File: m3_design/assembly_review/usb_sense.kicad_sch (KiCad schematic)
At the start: 3 parts

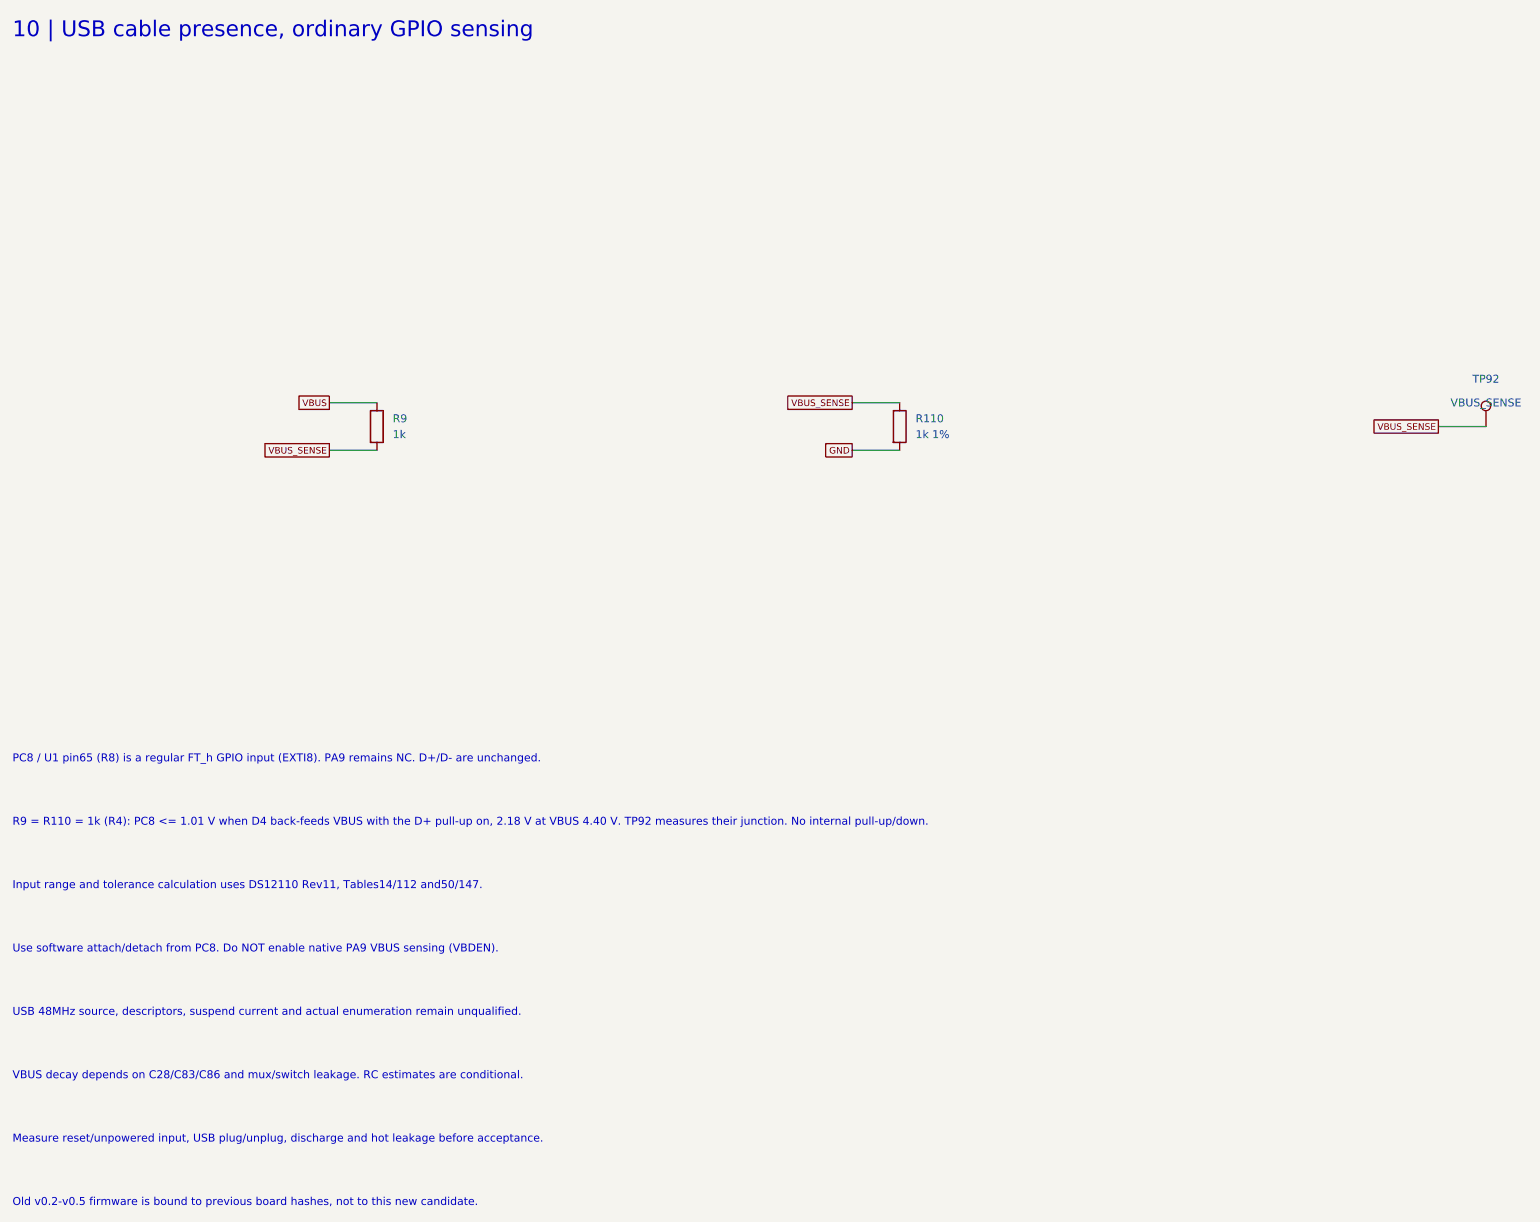
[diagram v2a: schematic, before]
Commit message: R10 requirements-audit cuts and GAP fixes before review round 9
Implement adopted AUD-1 through AUD-10 and GAP-1 through GAP-5 after the single-switch pass.
Remove the advisory pull-pin, redundant probes and GPS/radio IO LDO cells; qualify the smaller
AONR21357 pair, correct C120 voltage rating, standardize shared-code capacitor lands, simplify
slow returns and fire-only copper, localize U9 output protection and add exactly two U401 VIPPO vias.
Record physical-current timing, coupled fire/source budget, C84 manual fitting and narrowed gate scopes.

Board SHA-256: 877d01996a59e9dd5c6dbc367274bb9a323a13982d67960fe46df9b0ee53205d
Board: 46 x 90 mm, 4 layers, 2365477 bytes; 225 footprints, 883 straight tracks, 323 vias.
Netlist SHA-256: 0843da709e2d7a757e9b35cdff48158a54012c5353619cbf409ab961efd2c3ca
Two fresh complete passing builds are byte-identical. Schematic: 700 pins; 22 seeded faults detected.

Final unskipped tools/check.sh: exit 0
DRC violations 0  unconnected 0  schematic parity 0  ERC 0
metadata / 3D model audit: OK
silkscreen outside the board outline: 0 stroke points
fit check: OK (CAD envelopes only)
R10 CAD contract (full): OK
routing hygiene: 0 failing, 0 allowlisted, 0 leftovers recorded
actuator safety contract: OK
Fab manifest: OK; 5 outputs match current CAD and export inputs
Self-tests: shell 4, fit 24, paste 5, routing 59, R10 131; three NumPy cases rerun and passed.

Fab: 215 CPL rows, 82 BOM codes; orientation / paste / manifest pass. Hot-plug: 2304 required
cases plus convergence and controls pass (simulation / Inference). Plate f1 280.9 Hz (Inference).
Live JLC: $84.43 vs $84.41 target, 46 Extended codes; R430 / U4 short. Procurement exit 1 is a
disclosed OQ-3 / ordering deviation, not a CAD gate pass. No quote accepted or order placed.
Firmware, bench, thermal/transient correlation, process acceptance, installed RF immunity and physical fit unverified.

This preparatory pass earns no clean-review credit. Start fresh full ten-lens round 9 on th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
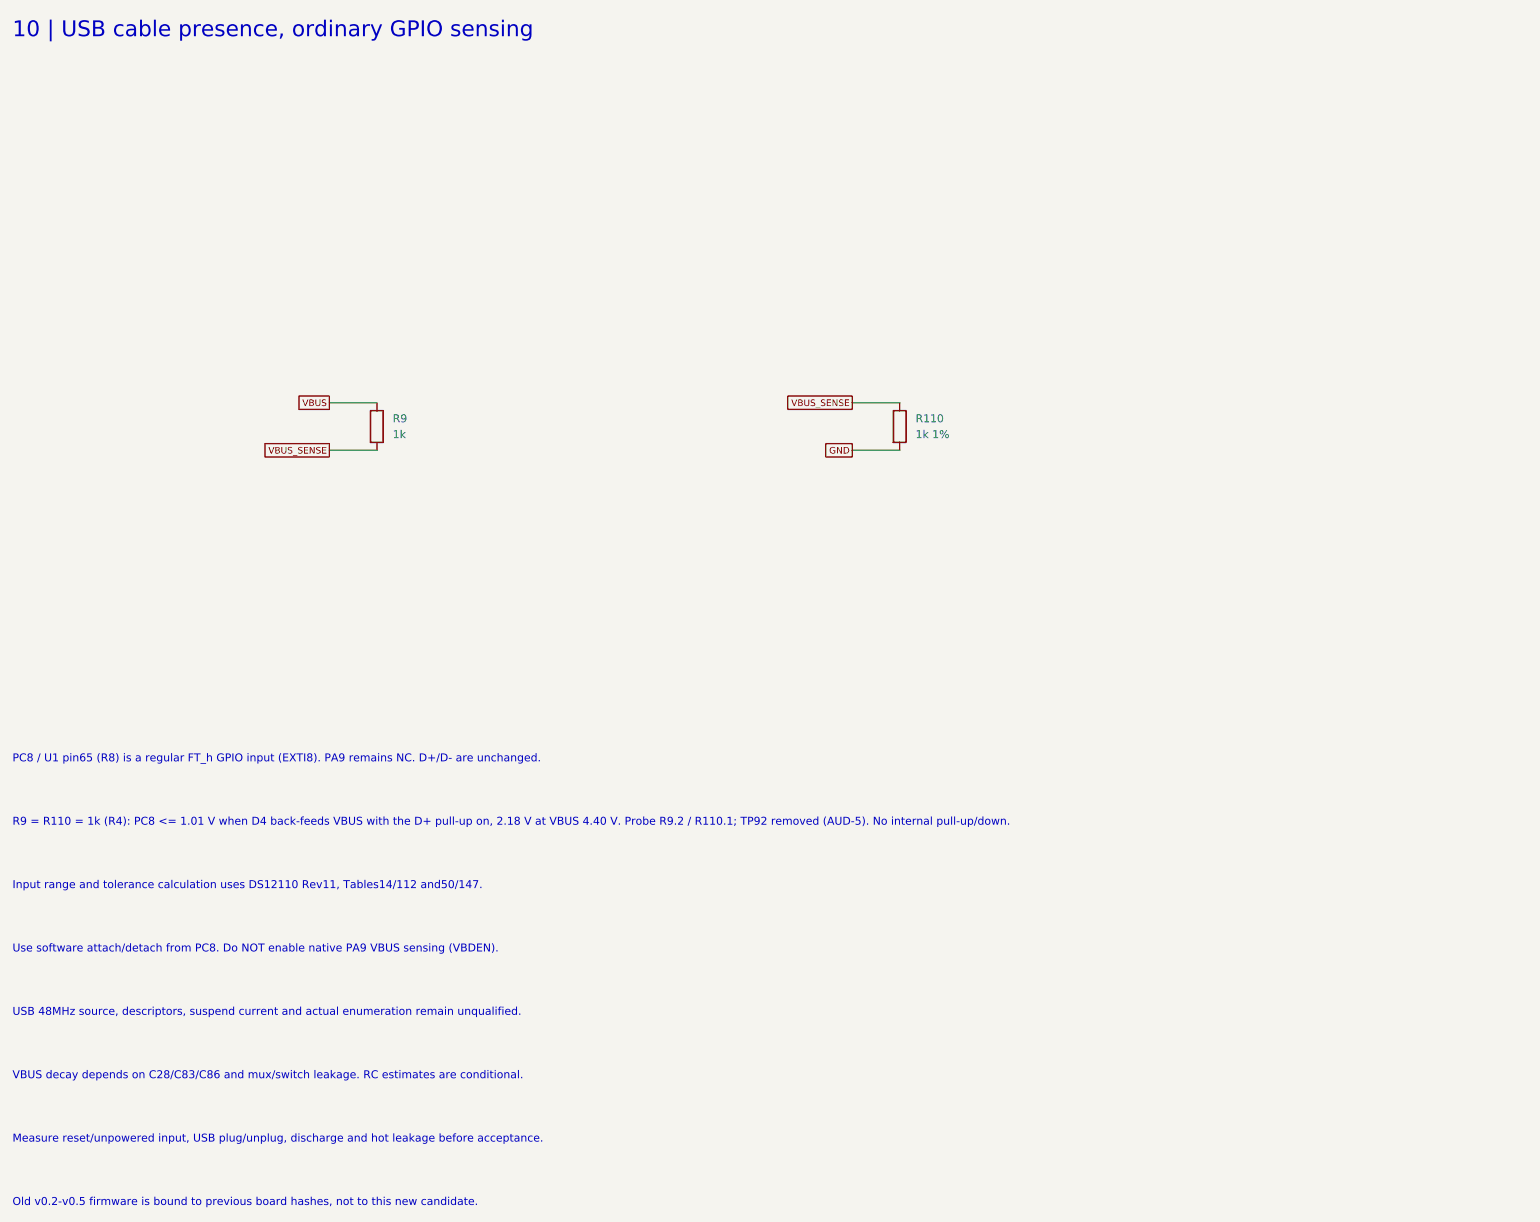
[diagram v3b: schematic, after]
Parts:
- removed TP92: VBUS_SENSE, rocket:M3_TestPad_1.5, symbol M3:TestPoint
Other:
- note added: "R9 = R110 = 1k (R4): PC8 <= 1.01 V when D4 back-feeds VBUS with the D+ pull-up on, 2.18 V at VBUS 4.40 V. Probe R9.2 / R110.1; TP92 removed (AUD-5). No internal pull-up/down."
- note removed: "R9 = R110 = 1k (R4): PC8 <= 1.01 V when D4 back-feeds VBUS with the D+ pull-up on, 2.18 V at VBUS 4.40 V. TP92 measures their junction. No internal pull-up/down."
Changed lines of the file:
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@@
-			(justify right))
-)
-	(symbol
-		(lib_id "M3:TestPoint")
-		(at 256.54 83.82 0)
-		(unit 1)
-		(in_bom no)
-		(on_board yes)
-		(dnp no)
-		(property "Reference" "TP92"
-			(at 256.54 76.19999999999999 0)
-			(effects
-				(font
-					(size 1.27 1.27))))
-		(property "Value" "VBUS_SENSE"
-			(at 256.54 80.00999999999999 0)
-			(effects
-				(font
-					(size 1.27 1.27))))
-		(property "Footprint" "rocket:M3_TestPad_1.5"
-			(at 256.54 83.82 0)
-			(hide yes)
-			(effects
-				(font
-					(size 1.27 1.27))))
-		(property "Datasheet" ""
-			(at 256.54 83.82 0)
-			(hide yes)
-			(effects
-				(font
-					(size 1.27 1.27))))
-		(property "LCSC" ""
-			(at 256.54 83.82 0)
-			(hide yes)
-			(effects
-				(font
-					(size 1.27 1.27))))
-		(instances
-			(project "m3"
-				(path "/6007a7db-6a58-5660-8beb-956dea045ff8/7323b515-8986-5814-85b5-9e04db992507"
-					(reference "TP92")
-					(unit 1)))))
-	(wire
-		(pts
-			(xy 256.54 83.82)
-			(xy 248.92000000000002 83.82))
-		(stroke
-			(width 0)
-			(type default))
-)
-	(global_label "VBUS_SENSE"
-		(shape passive)
-		(at 248.92000000000002 83.82 0)
-		(effects
-			(font
-				(size 1.05 1.05))
 			(justify right))
 )
@@
 			(justify left))
 )
-	(text "R9 = R110 = 1k (R4): PC8 <= 1.01 V when D4 back-feeds VBUS with the D+ pull-up on, 2.18 V at VBUS 4.40 V. TP92 measures their junction. No internal pull-up/down."
+	(text "R9 = R110 = 1k (R4): PC8 <= 1.01 V when D4 back-feeds VBUS with the D+ pull-up on, 2.18 V at VBUS 4.40 V. Probe R9.2 / R110.1; TP92 removed (AUD-5). No internal pull-up/down."
 		(at 20.32 147.32 0)
 		(effects
